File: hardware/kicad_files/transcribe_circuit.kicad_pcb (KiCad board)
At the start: 2 copper layers, 100 x 45 mm, 20 parts, among them J1 RS232_SERIAL, J2 MIDI_IN_TRS, J3 MIDI_OUT_TRS, J4 RS232_DSUB, J5 MIDI_IN_DIN, J6 MIDI_OUT_DIN, U1 ProMicro, U2 MAX232, U3 L78L33_TO92, U4 usbHostMini, U5 6N137

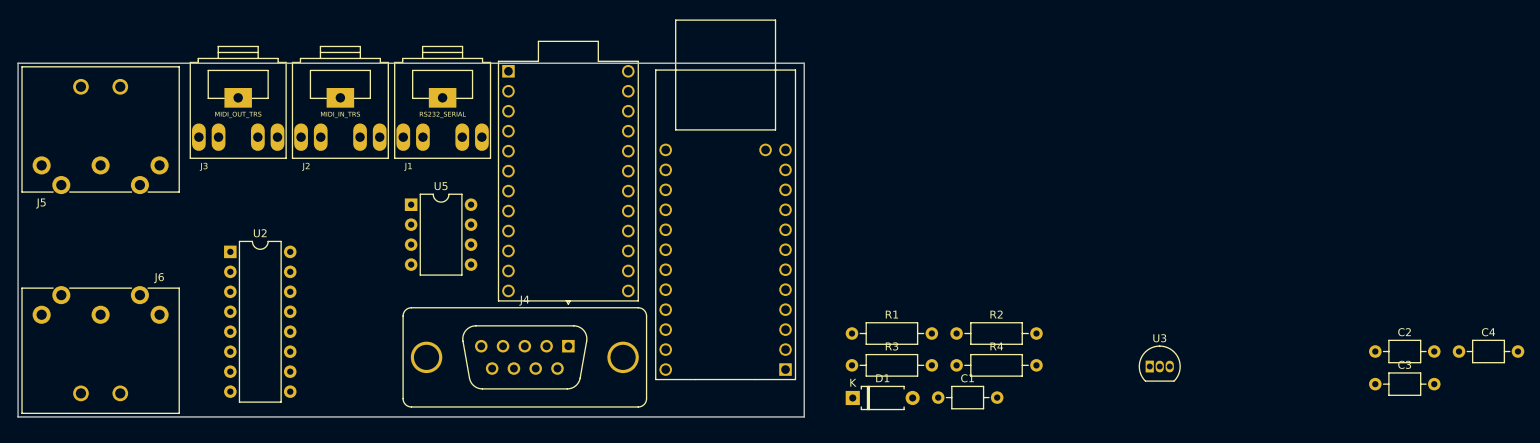
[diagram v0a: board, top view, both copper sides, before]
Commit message: chipping away at pcb layout
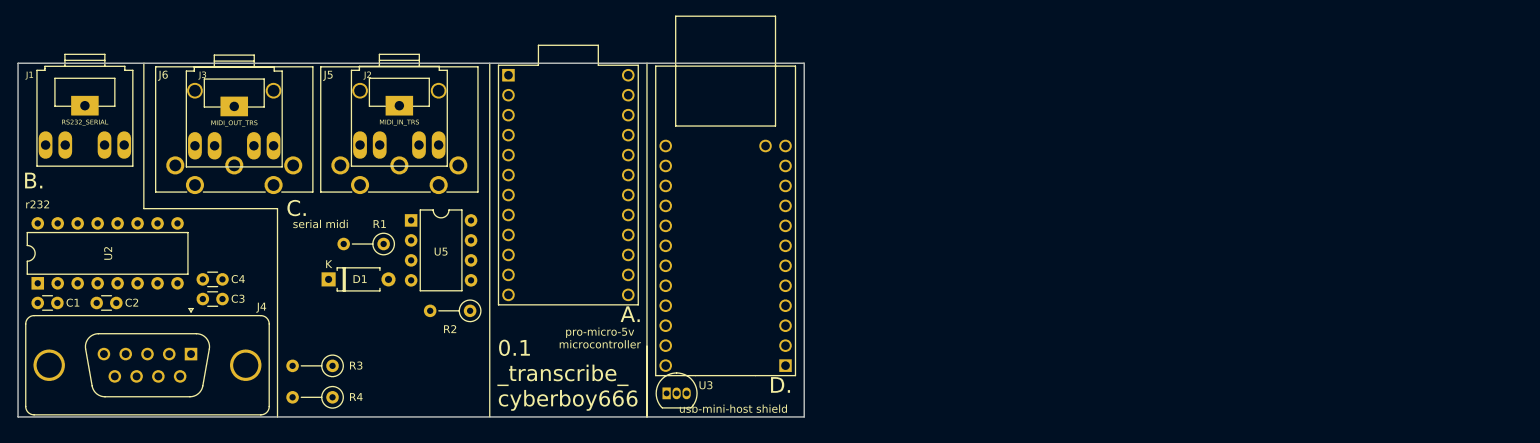
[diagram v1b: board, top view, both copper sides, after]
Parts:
- C1, C2, C3, C4: footprint Capacitor_THT:C_Axial_L3.8mm_D2.6mm_P7.50mm_Horizontal -> Capacitor_THT:C_Disc_D3.0mm_W1.6mm_P2.50mm
- J5, J6: footprint Connector_DIN:SDS-50J -> Connector_DIN:Tayda5pinMidi-A1010
- R1, R2, R3, R4: footprint Resistor_THT:R_Axial_DIN0207_L6.3mm_D2.5mm_P10.16mm_Horizontal -> Resistor_THT:R_Axial_DIN0207_L6.3mm_D2.5mm_P5.08mm_Vertical
- moved C2 162.8 mm to (-280.0, -759.5)
- moved C4 157.6 mm to (-264.0, -762.5), turned to 180 degrees
- moved C3 147.0 mm to (-264.0, -760.0), turned to 180 degrees
- moved C1 115.2 mm to (-287.5, -759.5)
- moved R4 79.5 mm to (-250.0, -747.5), turned to 180 degrees
- moved D1 68.4 mm to (-250.5, -762.5)
- moved R3 66.1 mm to (-250.0, -751.5), turned to 180 degrees
- moved R2 62.0 mm to (-232.5, -758.5), turned to 180 degrees
- moved U3 61.5 mm to (-207.5, -748.0)
- moved R1 60.7 mm to (-243.5, -767.0), turned to 180 degrees
- moved J4 48.0 mm to (-268.0, -753.0)
- moved J1 45.5 mm to (-281.5, -783.0)
- moved J5 38.0 mm to (-249.0, -777.0)
- moved U2 24.8 mm to (-287.5, -762.0), turned to 90 degrees
- moved J6 19.1 mm to (-270.0, -777.0), turned to 0 degrees
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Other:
- board text added: "0.1 _transcribe_ cyberboy666"
- board text added: "A."
- board text added: "B."
- board text added: "C."
- board text added: "D."
- board text added: "pro-micro-5v microcontroller"
- board text added: "r232"
- board text added: "serial midi"
- board text added: "usb-mini-host shield"

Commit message: wip
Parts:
- removed the J3 at (-262.5, -782.9)
- added C1: 100uf, Capacitor_THT:CP_Radial_D6.3mm_P2.50mm, F.Cu at (-227.0, -755.0)
- added J4: MIDI_IN_TRS, Connector_Audio:Tayda_3.5mm_stereo_TRS_jack_A-853, F.Cu at (-241.5, -783.0)
- added J6: MIDI_OUT_TRS, Connector_Audio:Tayda_3.5mm_stereo_TRS_jack_A-853, F.Cu at (-262.5, -783.0)
- added U5: usbHostMini, Module:usbHostMidi, F.Cu at (-199.9, -765.5)
- J1: value RS232_SERIAL -> europower; footprint Connector_Audio:Tayda_3.5mm_stereo_TRS_jack_A-853 -> Connector_PinHeader_2.54mm:PinHeader_2x08_P2.54mm_Vertical
- J2: value MIDI_IN_TRS -> RS232_SERIAL
- U4: value usbHostMini -> 4069; footprint Module:usbHostMidi -> Package_DIP:DIP-14_W7.62mm
- moved J1 77.2 mm to (-212.0, -749.5), turned to 270 degrees
- moved U4 66.7 mm to (-266.5, -760.0)
- moved J2 40.5 mm to (-282.0, -783.0)
- moved C3 12.0 mm to (-276.0, -760.0)
- moved D1 9.49 mm to (-247.5, -771.5), turned to 270 degrees
- moved C5 7.43 mm to (-271.0, -760.0)
- moved R2 6.00 mm to (-250.0, -753.5)
- moved R1 5.50 mm to (-250.0, -757.0)
- moved C4 3.54 mm to (-283.5, -760.0)
- moved C2 1.12 mm to (-288.5, -760.0)
- moved U6 1.00 mm to (-207.5, -747.0)
- moved U2 0.71 mm to (-288.0, -762.5)
- moved R3 0.50 mm to (-243.5, -766.5), turned to 90 degrees
- moved U1 0.32 mm to (-220.3, -774.4)
- renumbered C1 to C2, C2 to C4, C4 to C5, J4 to J3, J6 to J7, R3 to R1, R4 to R2, R1 to R3, R2 to R4, U5 to U3, U3 to U6
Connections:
- J1 pad 1: (no net) -> Net-(J1-Pad1)
- J1 pad 2: (no net) -> Net-(J1-Pad2)
- J1 pad 3: (no net) -> GND
- J1 pad 4: (no net) -> GND
- J1 pad 5: (no net) -> GND
- J3 pad 0: Net-(J4-Pad0) -> GND
- R2 pad 1: MIDI_SERIAL_OUT -> Net-(R2-Pad1)
- U1 pad 21: +5V -> Net-(U1-Pad21)
- U1 pad 24: Net-(U1-Pad24) -> +5V
- U4 pad 13: SS_HOST -> Net-(U4-Pad13)
- U4 pad 14: MOSI_HOST -> +5V
- U4 pad 2: Net-(U4-Pad2) -> Net-(R2-Pad1)
- U4 pad 3: RST_HOST -> MIDI_SERIAL_OUT
- U4 pad 4: GND -> Net-(U4-Pad1)
- U4 pad 7: Net-(U4-Pad7) -> GND
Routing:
- net MIDI_SERIAL_OUT: track 0.00 -> 71.9 mm
- net ALT_SERIAL_IN: track 0.00 -> 51.5 mm
- net ALT_SERIAL_OUT: track 0.00 -> 49.9 mm
- net MIDI_OUT_PLUS: track 0.00 -> 42.5 mm
- net RS_SERIAL_OUT: track 0.00 -> 40.5 mm
- net RST_HOST: track 0.00 -> 36.9 mm
- net MIDI_OUT_DATA: track 0.00 -> 36.4 mm
- net GND: track 0.00 -> 34.6 mm
- net MIDI_IN_DATA: track 0.00 -> 32.4 mm
- net RS_SERIAL_IN: track 0.00 -> 32.0 mm
- net MIDI_SERIAL_IN: track 0.00 -> 30.3 mm
- net MIDI_IN_PLUS: track 0.00 -> 24.5 mm
- net SS_HOST: track 0.00 -> 23.7 mm
- net Net-(R2-Pad1): track 0.00 -> 21.6 mm
- net MOSI_HOST: track 0.00 -> 18.1 mm
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- added copper zone on B.Cu, net +5V
- added copper zone on F.Cu, net GND
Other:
- board text added: "usb-host shield"
- board text added: "v0.1 _transcribe_ cyberboy666"
- board text removed: "0.1 _transcribe_ cyberboy666"
- board text removed: "usb-mini-host shield"

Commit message: small pcb fixes
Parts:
- added D2: 1N4148, Diode_THT:D_T-1_P5.08mm_Horizontal, F.Cu at (-220.5, -757.0)
- C1: footprint Capacitor_THT:CP_Radial_D6.3mm_P2.50mm -> Capacitor_THT:CP_Radial_D5.0mm_P2.50mm
- C2, C3, C4, C5: footprint Capacitor_THT:C_Disc_D3.0mm_W1.6mm_P2.50mm -> Capacitor_THT:C_Disc_D4.3mm_W1.9mm_P5.00mm
- D1: footprint Diode_THT:D_A-405_P7.62mm_Horizontal -> Diode_THT:D_T-1_P5.08mm_Horizontal
- J1: footprint Connector_PinHeader_2.54mm:PinHeader_2x08_P2.54mm_Vertical -> lib_fp:PinHeader_2x08_P2.54_Euro
- J2, J4, J6: footprint Connector_Audio:Tayda_3.5mm_stereo_TRS_jack_A-853 -> lib_fp:Tayda_3.5mm_stereo_TRS_jack_A-853
- J5, J7: footprint Connector_DIN:Tayda5pinMidi-A1010 -> lib_fp:Tayda5pinMidi-A1010
- moved C5 11.5 mm to (-259.5, -759.0)
- moved C3 9.06 mm to (-267.0, -759.0)
- moved C4 3.64 mm to (-280.0, -759.0)
- moved R3 2.50 mm to (-243.5, -764.0)
- moved U4 2.50 mm to (-266.5, -762.5)
- moved D1 2.42 mm to (-247.5, -769.1)
- moved R4 2.00 mm to (-232.5, -756.5)
- moved J3 1.50 mm to (-268.0, -751.5)
- moved U3 1.50 mm to (-240.0, -768.5)
- moved C2 1.41 mm to (-287.5, -759.0)
- moved J2 1.00 mm to (-282.0, -784.0)
- moved J4 1.00 mm to (-241.5, -784.0)
- moved J5 1.00 mm to (-249.0, -778.0)
- moved J6 1.00 mm to (-262.5, -784.0)
- moved J7 1.00 mm to (-270.0, -778.0)
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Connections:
- J1 pad 11: +5V -> Net-(D2-Pad2)
- J1 pad 12: +5V -> Net-(D2-Pad2)
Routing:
- net +5V: track 13.7 -> 164.3 mm
- net Net-(D2-Pad2): track 0.00 -> 14.9 mm
- net RS_SERIAL_IN: track 32.0 -> 43.3 mm
- net Net-(C5-Pad2): track 3.25 -> 12.9 mm
- net RS_SERIAL_OUT: track 40.5 -> 46.8 mm
- net GND: track 34.6 -> 28.7 mm
- net MIDI_IN_PLUS: track 24.5 -> 28.5 mm
- net MIDI_IN_DATA: track 32.4 -> 35.7 mm
- net Net-(C3-Pad2): track 13.2 -> 16.3 mm
- net MIDI_OUT_DATA: track 36.4 -> 39.1 mm
- net MIDI_SERIAL_OUT: track 71.9 -> 74.5 mm
- net ALT_SERIAL_OUT: track 49.9 -> 52.4 mm
- net 3.3v: track 14.8 -> 12.6 mm
- net MIDI_SERIAL_IN: track 30.3 -> 32.5 mm
- net MIDI_OUT_PLUS: track 42.5 -> 44.3 mm
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- added copper zone on B.Cu, net GND
- removed copper zone on B.Cu, net +5V
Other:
- board text added: "v0.2 _transcribe_ cyberboy666"
- board text removed: "v0.1 _transcribe_ cyberboy666"

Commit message: update circuit to v0.2
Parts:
- added J8: Conn_01x06, Connector_PinSocket_2.54mm:PinSocket_1x06_P2.54mm_Vertical, F.Cu at (-204.6, -788.0)
- J3: footprint Connector_Dsub:DSUB-9_Female_Vertical_P2.77x2.84mm_MountingHoles -> lib_fp:DSUB-9_Male_Vertical_Tayda
- moved J3 11.0 mm to (-279.0, -752.0)
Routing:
- net SKC_HOST: track 14.8 -> 34.3 mm
- net MISO_HOST: track 11.0 -> 26.9 mm
- net RST_HOST: track 36.9 -> 51.1 mm
- net MOSI_HOST: track 18.1 -> 30.4 mm
- net +5V: track 164.3 -> 174.2 mm
- net GND: track 28.7 -> 36.0 mm
- net RS_SERIAL_IN: track 43.3 -> 37.6 mm
- net RS_SERIAL_OUT: track 46.8 -> 47.8 mm

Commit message: refactored the code and updated circuit
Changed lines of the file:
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@@
     (pcbplotparams
       (layerselection 0x010fc_ffffffff)
-      (usegerberextensions false)
+      (usegerberextensions true)
       (usegerberattributes false)
       (usegerberadvancedattributes false)
@@
       (drillshape 0)
       (scaleselection 1)
-      (outputdirectory "../transcribe_0.2/"))
+      (outputdirectory "../transcribe_0.2b/"))
   )
   (net 0 "")
@@
     (descr "Diode, T-1 series, Axial, Horizontal, pin pitch=5.08mm, , length*diameter=3.2*2.6mm^2, , http://www.diodes.com/_files/packages/T-1.pdf")
     (tags "Diode T-1 series Axial Horizontal pin pitch 5.08mm  length 3.2mm diameter 2.6mm")
-    (fp_text reference D1 (at 2.54 -2.42 90) (layer F.SilkS)
+    (fp_text reference D1 (at 2.73 0.1 90) (layer F.SilkS)
       (effects (font (size 1 1) (thickness 0.15)))
     )
@@
     (descr "SDS-50J, standard DIN connector, 5 pins, midi")
     (tags "SDS-50J DIN 5-pins connector midi")
-    (fp_text reference J7 (at -1.5 -11.5) (layer F.SilkS)
+    (fp_text reference J7 (at -1.5 -10.8) (layer F.SilkS)
       (effects (font (size 1 1) (thickness 0.15)))
     )
@@
   (module lib_fp:Tayda_3.5mm_stereo_TRS_jack_A-853 (layer F.Cu)
     (at -241.5 -784)
-    (fp_text reference J4 (at -4.3 -5.8) (layer F.SilkS)
+    (fp_text reference J4 (at -5.15 -5.15) (layer F.SilkS)
       (effects (font (size 0.8 0.8) (thickness 0.15)))
     )
@@
     (descr "TO-92 leads in-line, narrow, oval pads, drill 0.75mm (see NXP sot054_po.pdf)")
     (tags "to-92 sc-43 sc-43a sot54 PA33 transistor")
-    (fp_text reference U6 (at 5 -1) (layer F.SilkS)
+    (fp_text reference U6 (at 5.2 -0.55) (layer F.SilkS)
       (effects (font (size 1 1) (thickness 0.15)))
     )
@@
       (effects (font (size 1 1) (thickness 0.15)))
     )
-    (fp_text user %R (at 1.27 -3.56) (layer F.Fab)
+    (fp_text user %R (at 5.15 -0.6) (layer F.Fab)
       (effects (font (size 1 1) (thickness 0.15)))
     )
@@
     (descr "CP, Radial series, Radial, pin pitch=2.50mm, , diameter=5mm, Electrolytic Capacitor")
     (tags "CP Radial series Radial pin pitch 2.50mm  diameter 5mm Electrolytic Capacitor")
-    (fp_text reference C1 (at 1.25 -3.75) (layer F.SilkS)
+    (fp_text reference C1 (at -1.6 -2.8) (layer F.SilkS)
       (effects (font (size 1 1) (thickness 0.15)))
     )
@@
     (descr "C, Disc series, Radial, pin pitch=5.00mm, , diameter*width=4.3*1.9mm^2, Capacitor, http://www.vishay.com/docs/45233/krseries.pdf")
     (tags "C Disc series Radial pin pitch 5.00mm  diameter 4.3mm width 1.9mm Capacitor")
-    (fp_text reference C2 (at 2.5 -2.2) (layer F.SilkS)
+    (fp_text reference C2 (at 2.55 -0.05) (layer F.SilkS)
       (effects (font (size 1 1) (thickness 0.15)))
     )
@@
     (descr "C, Disc series, Radial, pin pitch=5.00mm, , diameter*width=4.3*1.9mm^2, Capacitor, http://www.vishay.com/docs/45233/krseries.pdf")
     (tags "C Disc series Radial pin pitch 5.00mm  diameter 4.3mm width 1.9mm Capacitor")
-    (fp_text reference C3 (at 2.5 -2.2) (layer F.SilkS)
+    (fp_text reference C3 (at 2.5 -0.05) (layer F.SilkS)
       (effects (font (size 1 1) (thickness 0.15)))
     )
@@
     (descr "C, Disc series, Radial, pin pitch=5.00mm, , diameter*width=4.3*1.9mm^2, Capacitor, http://www.vishay.com/docs/45233/krseries.pdf")
     (tags "C Disc series Radial pin pitch 5.00mm  diameter 4.3mm width 1.9mm Capacitor")
-    (fp_text reference C4 (at 2.5 -2.2) (layer F.SilkS)
+    (fp_text reference C4 (at 2.6 0.05) (layer F.SilkS)
       (effects (font (size 1 1) (thickness 0.15)))
     )
@@
     (descr "C, Disc series, Radial, pin pitch=5.00mm, , diameter*width=4.3*1.9mm^2, Capacitor, http://www.vishay.com/docs/45233/krseries.pdf")
     (tags "C Disc series Radial pin pitch 5.00mm  diameter 4.3mm width 1.9mm Capacitor")
-    (fp_text reference C5 (at 2.5 -2.2) (layer F.SilkS)
+    (fp_text reference C5 (at 2.45 0.05) (layer F.SilkS)
       (effects (font (size 1 1) (thickness 0.15)))
     )
@@
     (descr "Diode, T-1 series, Axial, Horizontal, pin pitch=5.08mm, , length*diameter=3.2*2.6mm^2, , http://www.diodes.com/_files/packages/T-1.pdf")
     (tags "Diode T-1 series Axial Horizontal pin pitch 5.08mm  length 3.2mm diameter 2.6mm")
-    (fp_text reference D2 (at 2.54 -2.42) (layer F.SilkS)
+    (fp_text reference D2 (at 2.85 -0.05) (layer F.SilkS)
       (effects (font (size 1 1) (thickness 0.15)))
     )
@@
   (module lib_fp:Tayda_3.5mm_stereo_TRS_jack_A-853 (layer F.Cu)
     (at -282 -784)
-    (fp_text reference J2 (at -4.1 -5.7) (layer F.SilkS)
+    (fp_text reference J2 (at -5.15 -4.95) (layer F.SilkS)
       (effects (font (size 0.8 0.8) (thickness 0.15)))
     )
@@
     (descr "SDS-50J, standard DIN connector, 5 pins, midi")
     (tags "SDS-50J DIN 5-pins connector midi")
-    (fp_text reference J5 (at -1.5 -11.5) (layer F.SilkS)
+    (fp_text reference J5 (at -1.5 -11) (layer F.SilkS)
       (effects (font (size 1 1) (thickness 0.15)))
     )
@@
   (module lib_fp:Tayda_3.5mm_stereo_TRS_jack_A-853 (layer F.Cu)
     (at -262.5 -784)
-    (fp_text reference J6 (at -4.1 -5.8) (layer F.SilkS)
+    (fp_text reference J6 (at -5.2 -5.25) (layer F.SilkS)
       (effects (font (size 0.8 0.8) (thickness 0.15)))
     )

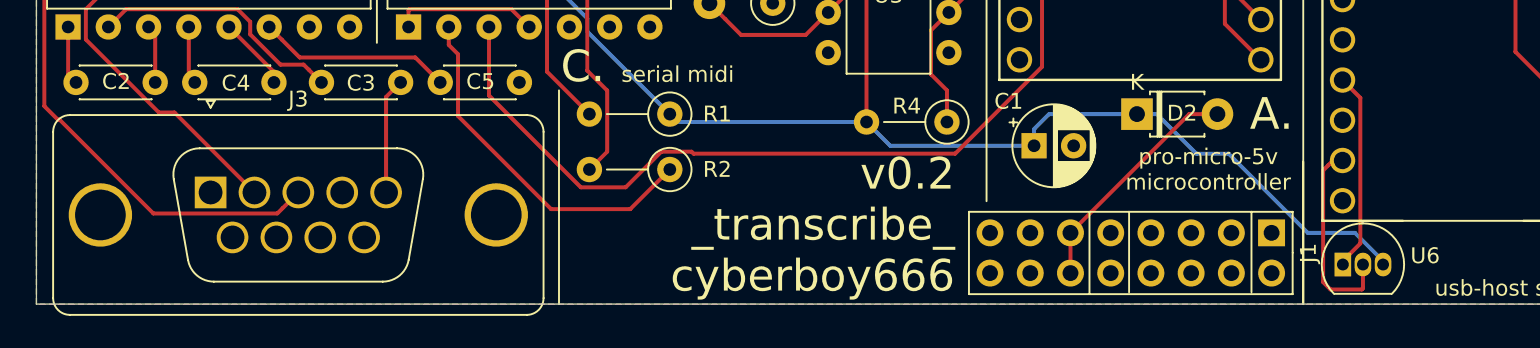
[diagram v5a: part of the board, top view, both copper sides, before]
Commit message: update circuit to 0.3 and add note to build guide for <=0.2
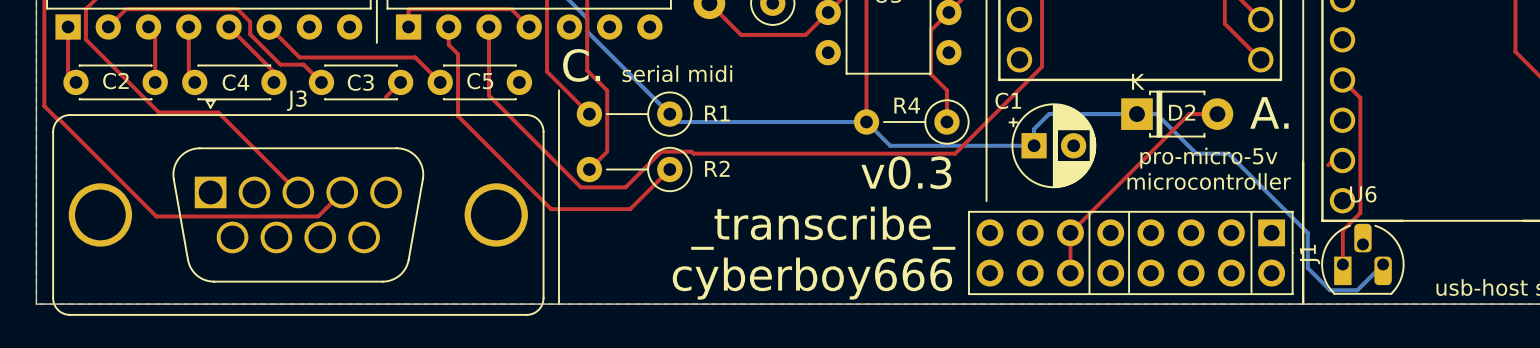
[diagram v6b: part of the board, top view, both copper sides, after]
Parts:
- U6: footprint Package_TO_SOT_THT:TO-92_Inline -> Package_TO_SOT_THT:TO-92_HandSolder
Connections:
- J2 pad RN: GND -> Net-(J2-PadRN)
- J2 pad TN: GND -> Net-(J2-PadTN)
- J3 pad 2: RS_SERIAL_IN -> RS_SERIAL_OUT
- J3 pad 3: RS_SERIAL_OUT -> RS_SERIAL_IN
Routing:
- net GND: track 36.0 -> 18.7 mm
- net RS_SERIAL_OUT: track 47.8 -> 50.7 mm
- net RS_SERIAL_IN: track 37.6 -> 40.4 mm
- net +5V: track 174.2 -> 176.9 mm
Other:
- board text added: "v0.3 _transcribe_ cyberboy666"
- board text removed: "v0.2 _transcribe_ cyberboy666"

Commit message: revised circuit v0.4
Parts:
- J2: value RS232_SERIAL -> stereo_jack_3.5mm; footprint lib_fp:Tayda_3.5mm_stereo_TRS_jack_A-853 -> lib_fp:horizontal_3.5mm_stereo_TRS_jack_A-853
- J3: value RS232_DSUB -> dsub9_socket; footprint lib_fp:DSUB-9_Male_Vertical_Tayda -> lib_fp:tht_DSUB-9_Vertical_Tayda
- J4: value MIDI_IN_TRS -> stereo_jack_3.5mm; footprint lib_fp:Tayda_3.5mm_stereo_TRS_jack_A-853 -> lib_fp:horizontal_3.5mm_stereo_TRS_jack_A-853
- J5: value MIDI_IN_DIN -> din5; footprint lib_fp:Tayda5pinMidi-A1010 -> lib_fp:horizontal_din5-A1010
- J6: value MIDI_OUT_TRS -> stereo_jack_3.5mm; footprint lib_fp:Tayda_3.5mm_stereo_TRS_jack_A-853 -> lib_fp:horizontal_3.5mm_stereo_TRS_jack_A-853
- J7: value MIDI_OUT_DIN -> din5; footprint lib_fp:Tayda5pinMidi-A1010 -> lib_fp:horizontal_din5-A1010
- U4: value 4069 -> CD4069
- U6: value L78L33_TO92 -> 78L33
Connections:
- U1 pad 1: MIDI_SERIAL_OUT -> ALT_SERIAL_OUT
- U1 pad 2: MIDI_SERIAL_IN -> ALT_SERIAL_IN
- U1 pad 7: ALT_SERIAL_IN -> MIDI_SERIAL_IN
- U1 pad 8: ALT_SERIAL_OUT -> MIDI_SERIAL_OUT
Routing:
- net MIDI_SERIAL_OUT: track 74.5 -> 56.1 mm
- net MIDI_SERIAL_IN: track 32.5 -> 19.4 mm
- net ALT_SERIAL_OUT: track 52.4 -> 63.4 mm
- net ALT_SERIAL_IN: track 51.5 -> 60.7 mm
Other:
- board text added: "_^ 03"
- board text added: "midi in"
- board text added: "midi out"
- board text added: "serial"
- board text added: "underscores.shop"
- board text added: "v0_4 _transcribe_ cyberboy666"
- board text removed: "v0.3 _transcribe_ cyberboy666"
